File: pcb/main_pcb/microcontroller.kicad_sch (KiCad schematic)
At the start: 20 parts, among them J1 Conn_01x05, J10 Conn_01x06_Male, J11 Conn_01x04, J2 Conn_01x05, J3 Conn_01x05, J4 Conn_01x05, J5 Conn_01x05, J6 Conn_01x05, J7 Conn_01x04, J8 Conn_01x06_Male, J9 Conn_01x04, U1 LSM6DSO, U2 Teensy_4.1, U3 DRV8833

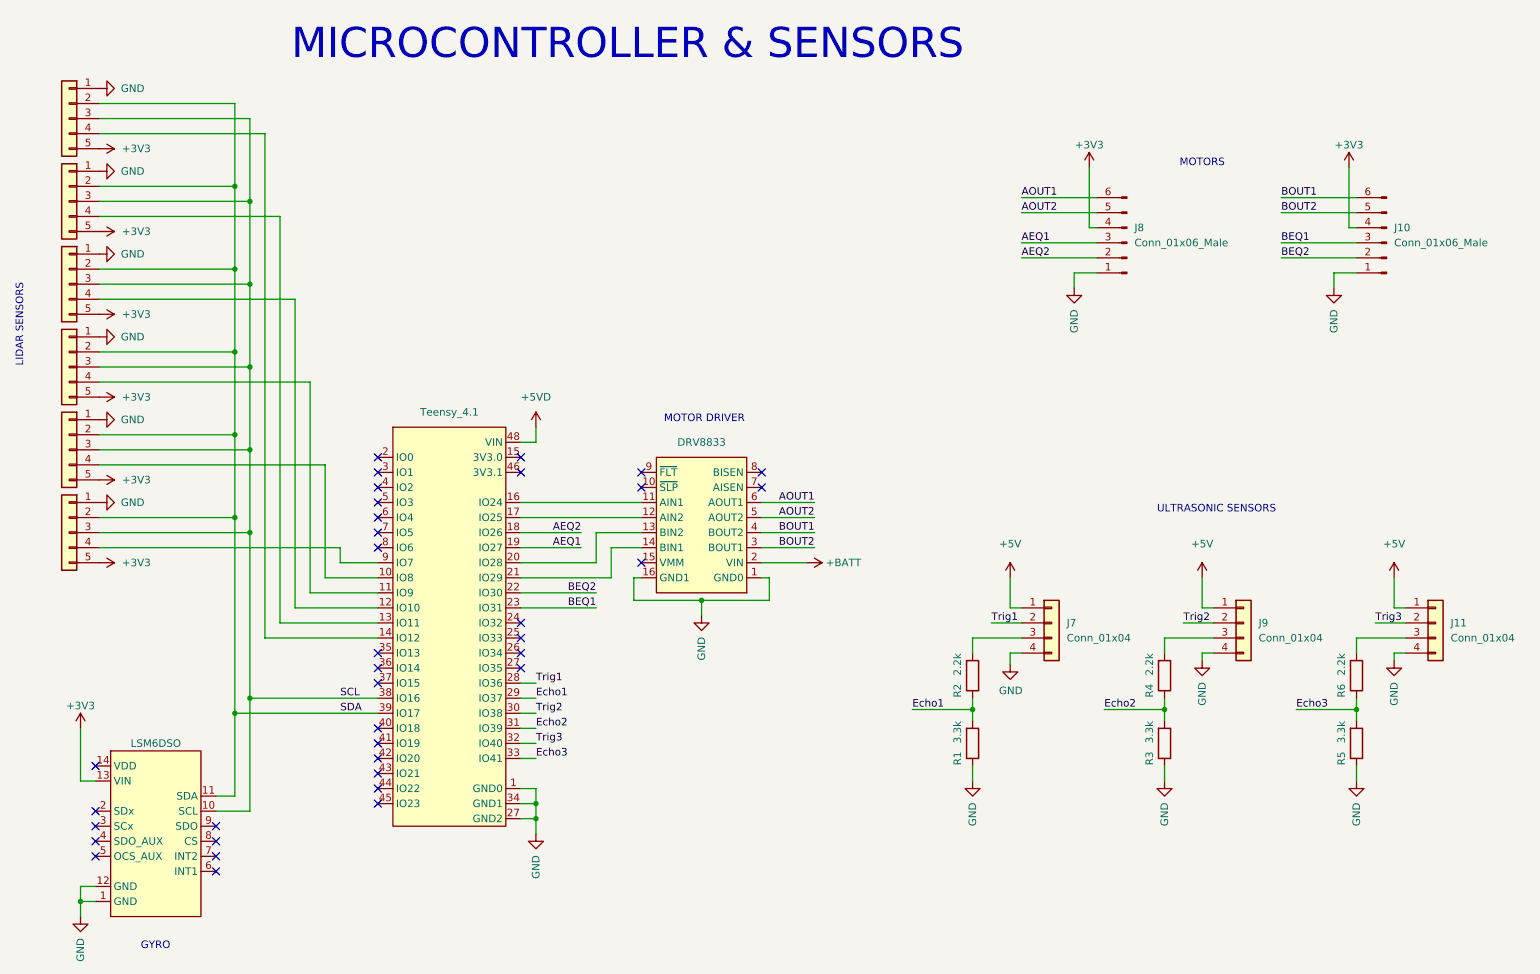
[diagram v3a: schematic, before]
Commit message: Reorganize Teensy connections for optimized routing
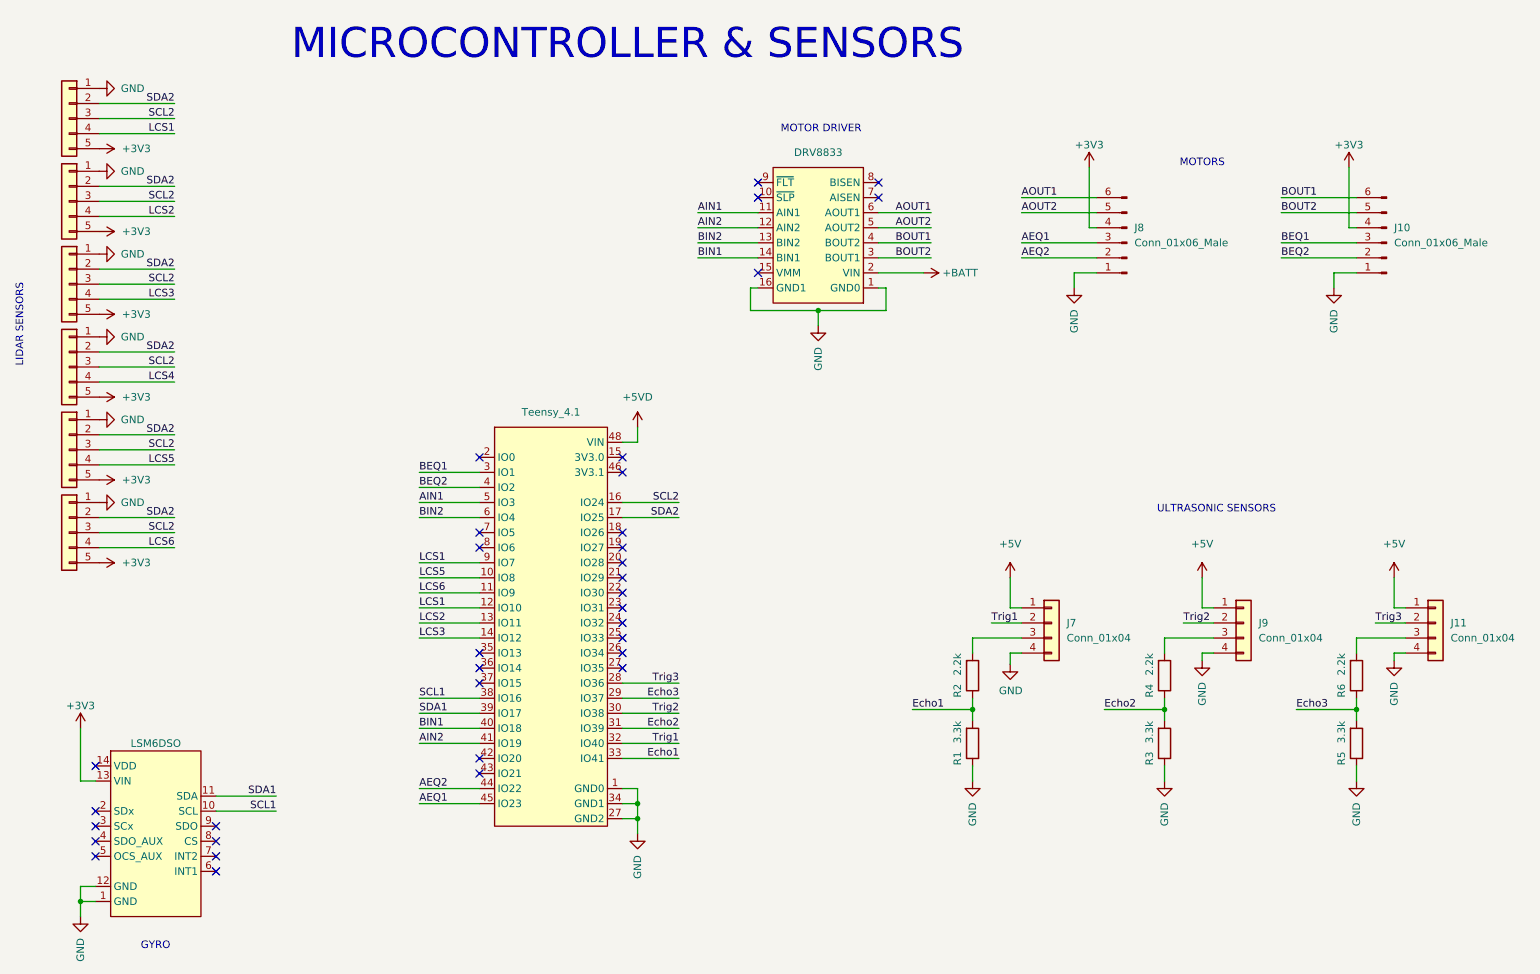
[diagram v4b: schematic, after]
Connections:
- net AEQ1: now also U2.45 (IO23); no longer U2.19 (IO27)
- net AEQ2: now also U2.44 (IO22); no longer U2.18 (IO26)
- net BEQ1: now also U2.3 (IO1); no longer U2.23 (IO31)
- net BEQ2: now also U2.4 (IO2); no longer U2.22 (IO30)
- net Echo1: now also U2.33 (IO41); no longer U2.29 (IO37)
- net Echo3: now also U2.29 (IO37); no longer U2.33 (IO41)
- net Trig1: now also U2.32 (IO40); no longer U2.28 (IO36)
- net Trig3: now also U2.28 (IO36); no longer U2.32 (IO40)
- net LCS2: now reaches J2.4 (Pin_4), U2.13 (IO11)
- net LCS1: now reaches U2.12 (IO10)
- net LCS1: now also J1.4 (Pin_4), U2.9 (IO7); no longer J3.4 (Pin_4)
- net LCS4: now reaches J4.4 (Pin_4)
- net LCS4: no longer U2.11 (IO9)
- net LCS3: now reaches U2.14 (IO12)
- net LCS3: now also J3.4 (Pin_4); no longer J1.4 (Pin_4)
- net LCS5: now reaches J5.4 (Pin_4), U2.10 (IO8)
- net AIN1: now reaches U3.11 (AIN1)
- net AIN1: now also U2.5 (IO3); no longer U2.16 (IO24)
- net AIN2: now reaches U3.12 (AIN2)
- net AIN2: now also U2.41 (IO19); no longer U2.17 (IO25)
- net at U2.20 (IO28): no longer U3.13 (BIN2)
- net at U2.21 (IO29): no longer U3.14 (BIN1)
- net BIN1: now reaches U2.40 (IO18)
- net BIN1: now also U3.14 (BIN1)
- net BIN2: now reaches U2.6 (IO4)
- net BIN2: now also U3.13 (BIN2)
- net LCS6: now reaches J6.4 (Pin_4)
- net LCS6: now also U2.11 (IO9); no longer U2.9 (IO7)
- net SCL renamed SCL2
- net SCL2: now also U2.16 (IO24); no longer U1.10 (SCL), U2.38 (IO16)
- net SDA renamed SDA2
- net SDA2: now also U2.17 (IO25); no longer U1.11 (SDA), U2.39 (IO17)
- new net SCL1: U1.10 (SCL), U2.38 (IO16)
- new net SDA1: U1.11 (SDA), U2.39 (IO17)
- no-connect marks 36 -> 34

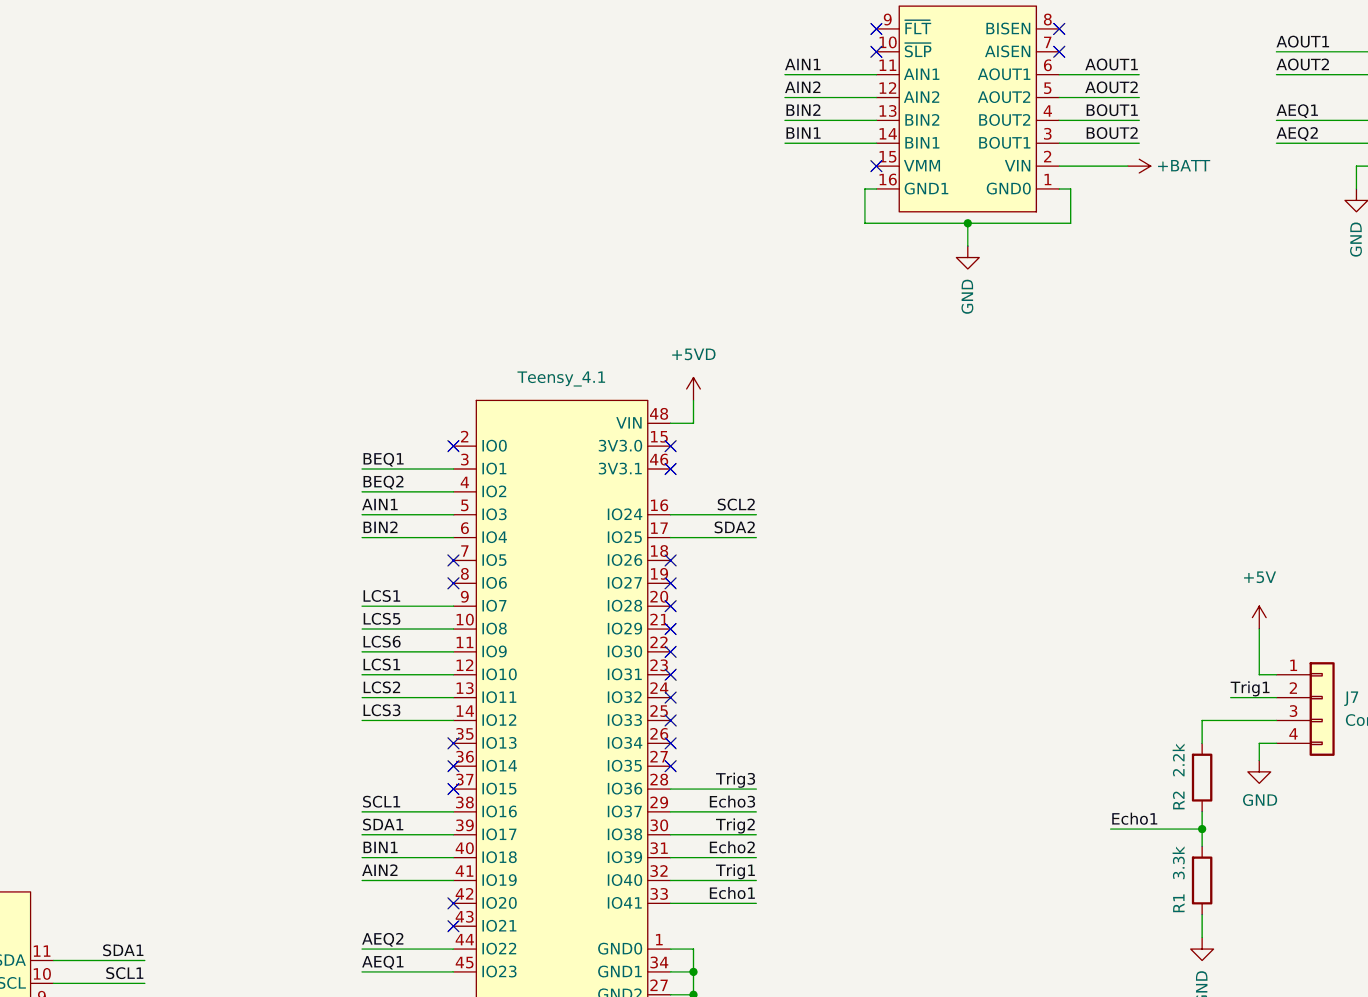
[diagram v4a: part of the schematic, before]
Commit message: Complete digital routing
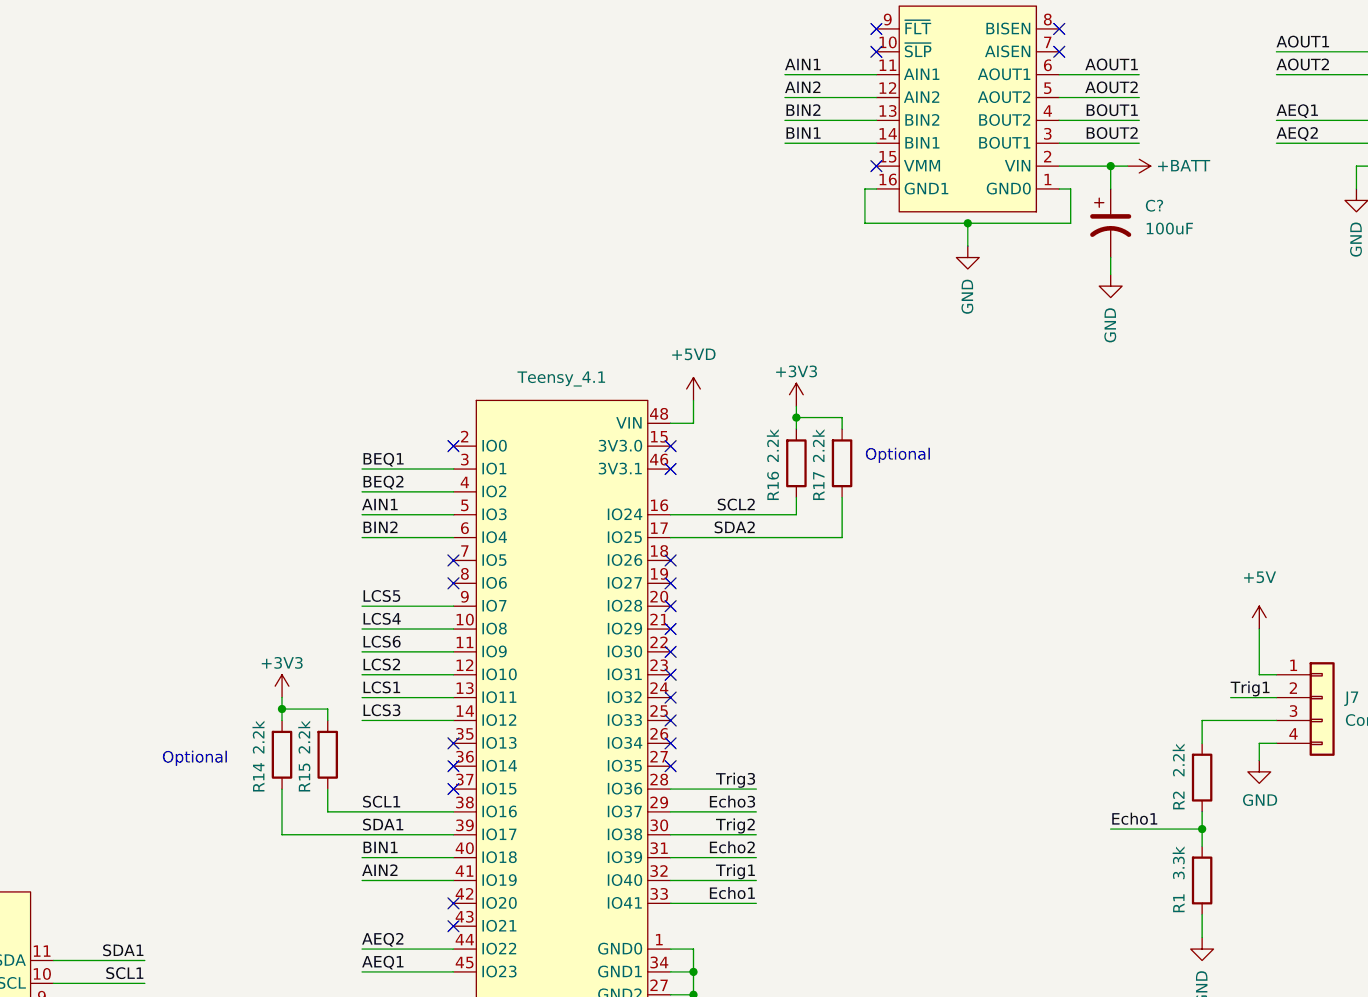
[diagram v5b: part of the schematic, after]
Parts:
- added C?: 100uF, Capacitor_SMD:CP_Elec_8x10.5, symbol Device:C_Polarized_US
- added R14, R15, R16, R17: 2.2k, Resistor_SMD:R_0603_1608Metric_Pad0.98x0.95mm_HandSolder, symbol Device:R
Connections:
- net +3V3: now also R14.2, R15.2, R16.2, R17.2
- net +BATT: now also C?.1
- net GND: now also C?.2
- net LCS1: now also U2.13 (IO11); no longer U2.12 (IO10), U2.9 (IO7)
- net LCS2: now also U2.12 (IO10); no longer U2.13 (IO11)
- net LCS4: now also U2.10 (IO8)
- net LCS5: now also U2.9 (IO7); no longer U2.10 (IO8)
- net SCL1: now also R15.1
- net SCL2: now also R16.1
- net SDA1: now also R14.1
- net SDA2: now also R17.1
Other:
- note added: "Optional"

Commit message: More routing
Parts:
- gave numbers to parts that had none: 1
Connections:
- net GND: now also U2.47 (GND2); no longer U2.27 (IO35)
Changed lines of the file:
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@@
     (effects (font (size 1.27 1.27)) (justify left bottom))
   )
-  (text "MOTOR DRIVER" (at 150.495 39.37 0)
+  (text "MOTOR DRIVER" (at 150.495 38.1 0)
     (effects (font (size 1.27 1.27)) (justify left bottom))
   )
@@
   (symbol (lib_id "Device:C_Polarized_US") (at 172.72 69.215 0) (unit 1)
     (in_bom yes) (on_board yes) (fields_autoplaced)
-    (property "Reference" "C?" (id 0) (at 176.53 67.3099 0)
+    (property "Reference" "C12" (id 0) (at 176.53 67.3099 0)
       (effects (font (size 1.27 1.27)) (justify left))
     )
@@
   (symbol (lib_id "sym_library:LSM6DSO") (at 45.085 152.4 0) (unit 1)
     (in_bom yes) (on_board yes)
-    (property "Reference" "U1" (id 0) (at 45.085 138.43 0)
-      (effects (font (size 1.27 1.27)) hide)
-    )
+    (property "Reference" "U1" (id 0) (at 45.085 138.43 0))
     (property "Value" "LSM6DSO" (id 1) (at 45.085 142.24 0))
     (property "Footprint" "custom_footprints:SENS_LSM6DSO_Pololu_2798" (id 2) (at 41.275 152.4 0)
@@
   (symbol (lib_id "sym_library:DRV8833") (at 156.845 61.595 180) (unit 1)
     (in_bom yes) (on_board yes)
-    (property "Reference" "U3" (id 0) (at 156.845 73.66 0)
-      (effects (font (size 1.27 1.27)) hide)
-    )
+    (property "Reference" "U3" (id 0) (at 156.845 40.005 0))
     (property "Value" "DRV8833" (id 1) (at 156.845 42.545 0))
     (property "Footprint" "custom_footprints:DRV_DRV8833_Pololu_2130" (id 2) (at 161.925 61.595 0)
@@
   (symbol (lib_id "sym_library:Teensy_4.1") (at 89.535 114.3 0) (unit 1)
     (in_bom yes) (on_board yes) (fields_autoplaced)
-    (property "Reference" "U2" (id 0) (at 111.76 83.82 0)
-      (effects (font (size 1.27 1.27)) hide)
-    )
+    (property "Reference" "U2" (id 0) (at 111.76 83.82 0))
     (property "Value" "Teensy_4.1" (id 1) (at 111.76 86.36 0))
     (property "Footprint" "custom_footprints:MCU_TEENSY41_PJRC" (id 2) (at 89.535 114.3 0)
@@
     (pin "25")
     (pin "26")
-    (pin "27")
     (pin "27")
     (pin "28")
@@
     (pin "45")
     (pin "46")
+    (pin "47")
     (pin "48")
     (pin "5")
@@
   (symbol (lib_id "power:GND") (at 172.72 74.93 0) (unit 1)
     (in_bom yes) (on_board yes)
-    (property "Reference" "#PWR?" (id 0) (at 172.72 81.28 0)
-      (effects (font (size 1.27 1.27)) hide)
-    )
+    (property "Reference" "#PWR0103" (id 0) (at 172.72 81.28 0)
+      (effects (font (size 1.27 1.27)) hide)
+    )

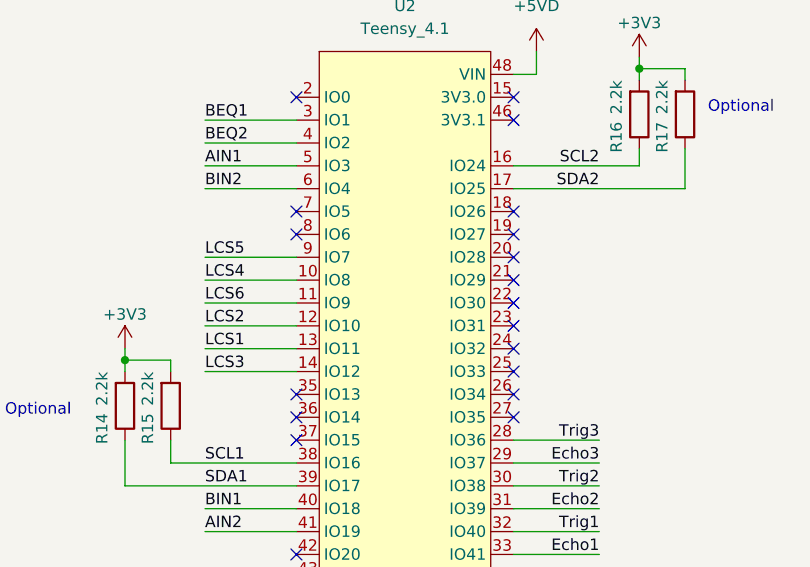
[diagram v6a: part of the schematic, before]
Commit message: Complete initial routing
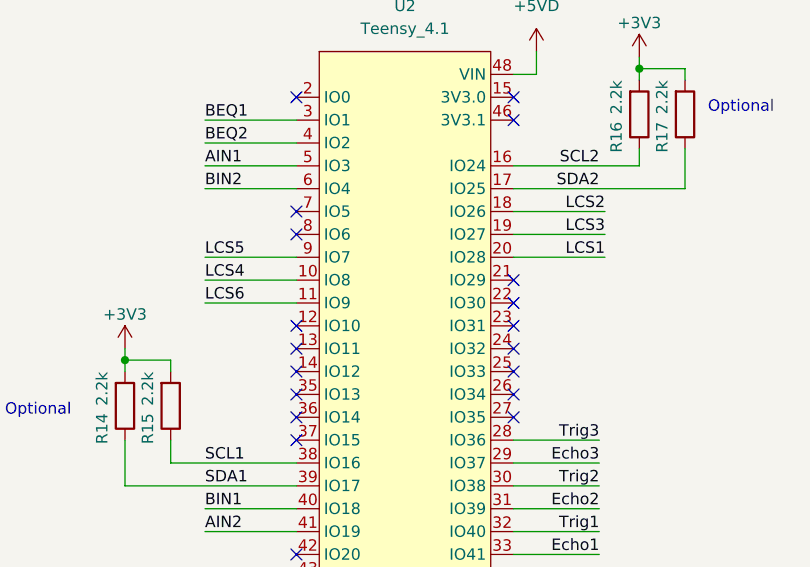
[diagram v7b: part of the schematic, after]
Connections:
- net LCS1: now also U2.20 (IO28); no longer U2.13 (IO11)
- net LCS2: now also U2.18 (IO26); no longer U2.12 (IO10)
- net LCS3: now also U2.19 (IO27); no longer U2.14 (IO12)
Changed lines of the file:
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@@
   (no_connect (at 34.925 158.75))
   (no_connect (at 34.925 146.05))
+  (no_connect (at 99.695 119.38))
   (no_connect (at 99.695 147.32))
   (no_connect (at 99.695 144.78))
@@
   (no_connect (at 123.825 96.52))
   (no_connect (at 99.695 132.08))
+  (no_connect (at 99.695 121.92))
+  (no_connect (at 99.695 124.46))
   (no_connect (at 146.685 50.165))
   (no_connect (at 123.825 127))
   (no_connect (at 99.695 93.98))
-  (no_connect (at 123.825 106.68))
-  (no_connect (at 123.825 109.22))
   (no_connect (at 123.825 119.38))
   (no_connect (at 123.825 114.3))
   (no_connect (at 123.825 116.84))
-  (no_connect (at 123.825 111.76))
   (no_connect (at 99.695 106.68))
   (no_connect (at 34.925 161.29))
@@
     (stroke (width 0) (type default) (color 0 0 0 0))
   )
-  (wire (pts (xy 89.535 121.92) (xy 99.695 121.92))
+  (wire (pts (xy 133.985 111.76) (xy 123.825 111.76))
     (stroke (width 0) (type default) (color 0 0 0 0))
   )
@@
     (stroke (width 0) (type default) (color 0 0 0 0))
   )
-  (wire (pts (xy 99.695 124.46) (xy 89.535 124.46))
+  (wire (pts (xy 123.825 109.22) (xy 133.985 109.22))
     (stroke (width 0) (type default) (color 0 0 0 0))
   )
@@
     (stroke (width 0) (type default) (color 0 0 0 0))
   )
-  (wire (pts (xy 99.695 119.38) (xy 89.535 119.38))
+  (wire (pts (xy 123.825 106.68) (xy 133.985 106.68))
     (stroke (width 0) (type default) (color 0 0 0 0))
   )
@@
     (effects (font (size 1.27 1.27)) (justify right bottom))
   )
-  (label "LCS2" (at 89.535 119.38 0)
-    (effects (font (size 1.27 1.27)) (justify left bottom))
+  (label "LCS2" (at 133.985 106.68 180)
+    (effects (font (size 1.27 1.27)) (justify right bottom))
   )
   (label "AOUT1" (at 175.895 52.705 180)
@@
     (effects (font (size 1.27 1.27)) (justify right bottom))
   )
-  (label "LCS1" (at 89.535 121.92 0)
-    (effects (font (size 1.27 1.27)) (justify left bottom))
+  (label "LCS1" (at 133.985 111.76 180)
+    (effects (font (size 1.27 1.27)) (justify right bottom))
   )
   (label "Trig2" (at 218.44 121.92 0)
@@
     (effects (font (size 1.27 1.27)) (justify right bottom))
   )
-  (label "LCS3" (at 89.535 124.46 0)
-    (effects (font (size 1.27 1.27)) (justify left bottom))
+  (label "LCS3" (at 133.985 109.22 180)
+    (effects (font (size 1.27 1.27)) (justify right bottom))
   )
   (symbol (lib_id "Connector_Generic:Conn_01x05") (at 30.48 50.8 0) (mirror y) (unit 1)

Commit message: Complete routing and Silkscreen
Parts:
- added D5, D6, D7, D8: LED, LED_THT:LED_D5.0mm, symbol Device:LED
- added R18, R19, R20, R21: 470, Resistor_SMD:R_0603_1608Metric_Pad0.98x0.95mm_HandSolder, symbol Device:R
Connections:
- net GND: now also R18.1, R19.1, R20.1, R21.1
- net LED2: now reaches U2.12 (IO10)
- net LED2: now also D7.2 (A)
- net LED3: now reaches U2.13 (IO11)
- net LED3: now also D8.2 (A)
- net LED0: now reaches U2.7 (IO5)
- net LED0: now also D5.2 (A)
- net LED1: now reaches U2.8 (IO6)
- net LED1: now also D6.2 (A)
- new net: D6.1 (K), R19.2
- new net: D7.1 (K), R20.2
- new net: D8.1 (K), R21.2
- new net: D5.1 (K), R18.2
- no-connect marks 34 -> 30
